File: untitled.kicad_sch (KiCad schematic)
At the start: 6 parts, among them J10 Conn_01x04_Male, J11 Conn_01x04_Male, J2 Conn_01x07_Male, J3 Conn_01x08_Male, J8 Conn_01x05_Male, J9 Conn_01x07_Male

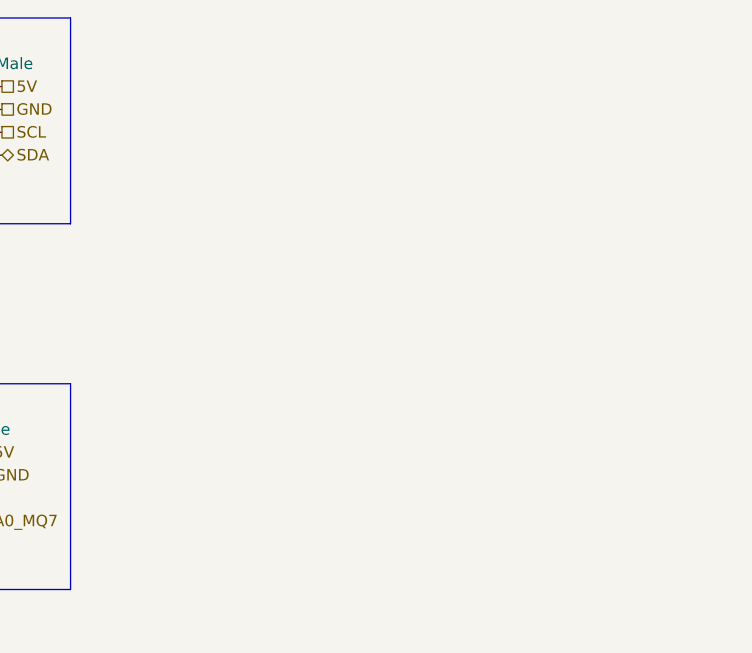
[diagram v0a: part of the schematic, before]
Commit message: Added some MQs
needs to be further investigated - to check if it is worth it to install also plain MQ
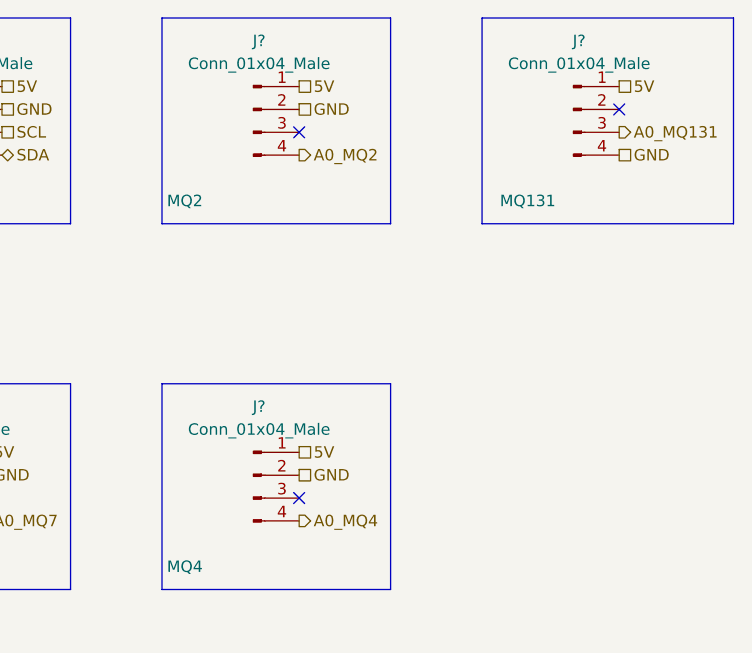
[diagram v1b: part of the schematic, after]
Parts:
- added J? (x3): Conn_01x04_Male, Connector_PinSocket_2.54mm:PinSocket_1x04_P2.54mm_Vertical, symbol Connector:Conn_01x04_Male
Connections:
- net 5V: now also J?.1 (Pin_1), J?.1 (Pin_1), J?.1 (Pin_1)
- net GND: now also J?.2 (Pin_2), J?.2 (Pin_2), J?.4 (Pin_4)
- new net A0_MQ131: J?.3 (Pin_3)
- new net A0_MQ2: J?.4 (Pin_4)
- new net A0_MQ4: J?.4 (Pin_4)
- no-connect marks 12 -> 15
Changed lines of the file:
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@@
   (no_connect (at 45.72 88.9))
   (no_connect (at 45.72 91.44))
+  (no_connect (at 147.32 43.18))
   (no_connect (at 76.2 43.18))
   (no_connect (at 43.18 53.34))
   (no_connect (at 43.18 40.64))
   (no_connect (at 76.2 88.9))
+  (no_connect (at 147.32 83.82))
+  (no_connect (at 182.88 40.64))
   (no_connect (at 76.2 91.44))
   (no_connect (at 111.76 83.82))
@@
     (stroke (width 0) (type default) (color 0 0 0 0))
   )
+  (polyline (pts (xy 157.48 53.34) (xy 157.48 30.48))
+    (stroke (width 0) (type default) (color 0 0 0 0))
+  )
+  (polyline (pts (xy 157.48 93.98) (xy 157.48 71.12))
+    (stroke (width 0) (type default) (color 0 0 0 0))
+  )
+  (polyline (pts (xy 132.08 71.12) (xy 132.08 93.98))
+    (stroke (width 0) (type default) (color 0 0 0 0))
+  )
   (polyline (pts (xy 60.96 68.58) (xy 60.96 96.52))
     (stroke (width 0) (type default) (color 0 0 0 0))
   )
+  (polyline (pts (xy 132.08 93.98) (xy 157.48 93.98))
+    (stroke (width 0) (type default) (color 0 0 0 0))
+  )
   (polyline (pts (xy 60.96 58.42) (xy 83.82 58.42))
     (stroke (width 0) (type default) (color 0 0 0 0))
@@
     (stroke (width 0) (type default) (color 0 0 0 0))
   )
+  (polyline (pts (xy 132.08 53.34) (xy 157.48 53.34))
+    (stroke (width 0) (type default) (color 0 0 0 0))
+  )
   (polyline (pts (xy 96.52 71.12) (xy 96.52 93.98))
     (stroke (width 0) (type default) (color 0 0 0 0))
@@
     (stroke (width 0) (type default) (color 0 0 0 0))
   )
+  (polyline (pts (xy 167.64 53.34) (xy 195.58 53.34))
+    (stroke (width 0) (type default) (color 0 0 0 0))
+  )
   (polyline (pts (xy 99.06 30.48) (xy 99.06 53.34))
     (stroke (width 0) (type default) (color 0 0 0 0))
@@
     (stroke (width 0) (type default) (color 0 0 0 0))
   )
+  (polyline (pts (xy 132.08 30.48) (xy 157.48 30.48))
+    (stroke (width 0) (type default) (color 0 0 0 0))
+  )
   (polyline (pts (xy 60.96 58.42) (xy 60.96 30.48))
     (stroke (width 0) (type default) (color 0 0 0 0))
   )
+  (polyline (pts (xy 195.58 53.34) (xy 195.58 30.48))
+    (stroke (width 0) (type default) (color 0 0 0 0))
+  )
   (polyline (pts (xy 86.36 96.52) (xy 60.96 96.52))
     (stroke (width 0) (type default) (color 0 0 0 0))
@@
     (stroke (width 0) (type default) (color 0 0 0 0))
   )
+  (polyline (pts (xy 132.08 71.12) (xy 157.48 71.12))
+    (stroke (width 0) (type default) (color 0 0 0 0))
+  )
   (polyline (pts (xy 30.48 68.58) (xy 30.48 99.06))
     (stroke (width 0) (type default) (color 0 0 0 0))
@@
     (stroke (width 0) (type default) (color 0 0 0 0))
   )
+  (polyline (pts (xy 132.08 30.48) (xy 132.08 53.34))
+    (stroke (width 0) (type default) (color 0 0 0 0))
+  )
   (polyline (pts (xy 53.34 68.58) (xy 30.48 68.58))
     (stroke (width 0) (type default) (color 0 0 0 0))
   )
+  (polyline (pts (xy 167.64 30.48) (xy 195.58 30.48))
+    (stroke (width 0) (type default) (color 0 0 0 0))
+  )
+  (polyline (pts (xy 167.64 30.48) (xy 167.64 53.34))
+    (stroke (width 0) (type default) (color 0 0 0 0))
+  )
   (polyline (pts (xy 53.34 58.42) (xy 27.94 58.42))
     (stroke (width 0) (type default) (color 0 0 0 0))
@@
     (effects (font (size 1.27 1.27)) (justify left))
   )
+  (hierarchical_label "A0_MQ4" (shape output) (at 147.32 86.36 0)
+    (effects (font (size 1.27 1.27)) (justify left))
+  )
   (hierarchical_label "5V" (shape passive) (at 114.3 38.1 0)
     (effects (font (size 1.27 1.27)) (justify left))
   )
+  (hierarchical_label "A0_MQ131" (shape output) (at 182.88 43.18 0)
+    (effects (font (size 1.27 1.27)) (justify left))
+  )
+  (hierarchical_label "GND" (shape passive) (at 147.32 81.28 0)
+    (effects (font (size 1.27 1.27)) (justify left))
+  )
   (hierarchical_label "5V" (shape passive) (at 111.76 78.74 0)
     (effects (font (size 1.27 1.27)) (justify left))
@@
     (effects (font (size 1.27 1.27)) (justify left))
   )
+  (hierarchical_label "A0_MQ2" (shape output) (at 147.32 45.72 0)
+    (effects (font (size 1.27 1.27)) (justify left))
+  )
   (hierarchical_label "5V" (shape passive) (at 76.2 76.2 0)
     (effects (font (size 1.27 1.27)) (justify left))
@@
     (effects (font (size 1.27 1.27)) (justify left))
   )
+  (hierarchical_label "5V" (shape passive) (at 147.32 38.1 0)
+    (effects (font (size 1.27 1.27)) (justify left))
+  )
+  (hierarchical_label "5V" (shape passive) (at 182.88 38.1 0)
+    (effects (font (size 1.27 1.27)) (justify left))
+  )
   (hierarchical_label "5V" (shape passive) (at 43.18 38.1 0)
     (effects (font (size 1.27 1.27)) (justify left))
@@
     (effects (font (size 1.27 1.27)) (justify left))
   )
+  (hierarchical_label "5V" (shape passive) (at 147.32 78.74 0)
+    (effects (font (size 1.27 1.27)) (justify left))
+  )
+  (hierarchical_label "GND" (shape passive) (at 182.88 45.72 0)
+    (effects (font (size 1.27 1.27)) (justify left))
+  )
   (hierarchical_label "SDA" (shape bidirectional) (at 114.3 45.72 0)
     (effects (font (size 1.27 1.27)) (justify left))
   )
   (hierarchical_label "GND" (shape passive) (at 76.2 45.72 0)
+    (effects (font (size 1.27 1.27)) (justify left))
+  )
+  (hierarchical_label "GND" (shape passive) (at 147.32 40.64 0)
     (effects (font (size 1.27 1.27)) (justify left))
   )
@@
     (pin "4")
     (pin "5")
+  )
+  (symbol (lib_id "Connector:Conn_01x04_Male") (at 177.8 40.64 0) (unit 1)
+    (in_bom yes) (on_board yes)
+    (property "Reference" "J?" (id 0) (at 178.435 33.02 0))
+    (property "Value" "Conn_01x04_Male" (id 1) (at 178.435 35.56 0))
+    (property "Footprint" "Connector_PinSocket_2.54mm:PinSocket_1x04_P2.54mm_Vertical" (id 2) (at 177.8 40.64 0)
+      (effects (font (size 1.27 1.27)) hide)
+    )
+    (property "Datasheet" "~" (id 3) (at 177.8 40.64 0)
+      (effects (font (size 1.27 1.27)) hide)
+    )
+    (property "Purpose" "MQ131" (id 4) (at 172.72 50.8 0))
+    (pin "1")
+    (pin "2")
+    (pin "3")
+    (pin "4")
   )
   (symbol (lib_id "Connector:Conn_01x07_Male") (at 38.1 45.72 0) (unit 1)
@@
     (pin "7")
   )
+  (symbol (lib_id "Connector:Conn_01x04_Male") (at 142.24 81.28 0) (unit 1)
+    (in_bom yes) (on_board yes)
+    (property "Reference" "J?" (id 0) (at 142.875 73.66 0))
+    (property "Value" "Conn_01x04_Male" (id 1) (at 142.875 76.2 0))
+    (property "Footprint" "Connector_PinSocket_2.54mm:PinSocket_1x04_P2.54mm_Vertical" (id 2) (at 142.24 81.28 0)
+      (effects (font (size 1.27 1.27)) hide)
+    )
+    (property "Datasheet" "~" (id 3) (at 142.24 81.28 0)
+      (effects (font (size 1.27 1.27)) hide)
+    )
+    (property "Purpose" "MQ4" (id 4) (at 134.62 91.44 0))
+    (pin "1")
+    (pin "2")
+    (pin "3")
+    (pin "4")
+  )
   (symbol (lib_id "Connector:Conn_01x04_Male") (at 106.68 81.28 0) (unit 1)
     (in_bom yes) (on_board yes)
@@
     (pin "1")
     (pin "2")
+    (pin "3")
+    (pin "4")
+  )
+  (symbol (lib_id "Connector:Conn_01x04_Male") (at 142.24 40.64 0) (unit 1)
+    (in_bom yes) (on_board yes)
+    (property "Reference" "J?" (id 0) (at 142.875 33.02 0))
+    (property "Value" "Conn_01x04_Male" (id 1) (at 142.875 35.56 0))
+    (property "Footprint" "Connector_PinSocket_2.54mm:PinSocket_1x04_P2.54mm_Vertical" (id 2) (at 142.24 40.64 0)
+      (effects (font (size 1.27 1.27)) hide)
+    )
+    (property "Datasheet" "~" (id 3) (at 142.24 40.64 0)
+      (effects (font (size 1.27 1.27)) hide)
+    )
+    (property "Purpose" "MQ2" (id 4) (at 134.62 50.8 0))
+    (pin "1")
+    (pin "2")

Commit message: Rearrangement
in order to fit all the new female pin sockets and fit all into a smaller PCB
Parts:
- gave numbers to parts that had none: 3
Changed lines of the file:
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@@
   (symbol (lib_id "Connector:Conn_01x04_Male") (at 177.8 40.64 0) (unit 1)
     (in_bom yes) (on_board yes)
-    (property "Reference" "J?" (id 0) (at 178.435 33.02 0))
+    (property "Reference" "J14" (id 0) (at 178.435 33.02 0))
     (property "Value" "Conn_01x04_Male" (id 1) (at 178.435 35.56 0))
     (property "Footprint" "Connector_PinSocket_2.54mm:PinSocket_1x04_P2.54mm_Vertical" (id 2) (at 177.8 40.64 0)
@@
   (symbol (lib_id "Connector:Conn_01x04_Male") (at 142.24 81.28 0) (unit 1)
     (in_bom yes) (on_board yes)
-    (property "Reference" "J?" (id 0) (at 142.875 73.66 0))
+    (property "Reference" "J13" (id 0) (at 142.875 73.66 0))
     (property "Value" "Conn_01x04_Male" (id 1) (at 142.875 76.2 0))
     (property "Footprint" "Connector_PinSocket_2.54mm:PinSocket_1x04_P2.54mm_Vertical" (id 2) (at 142.24 81.28 0)
@@
   (symbol (lib_id "Connector:Conn_01x04_Male") (at 142.24 40.64 0) (unit 1)
     (in_bom yes) (on_board yes)
-    (property "Reference" "J?" (id 0) (at 142.875 33.02 0))
+    (property "Reference" "J12" (id 0) (at 142.875 33.02 0))
     (property "Value" "Conn_01x04_Male" (id 1) (at 142.875 35.56 0))
     (property "Footprint" "Connector_PinSocket_2.54mm:PinSocket_1x04_P2.54mm_Vertical" (id 2) (at 142.24 40.64 0)

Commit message: Design tweaking
staging of all the modifications needed , in order to cover the needs of all the power board
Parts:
- removed J11, J13: Conn_01x04_Male, Connector_PinSocket_2.54mm:PinSocket_1x04_P2.54mm_Vertical, symbol Connector:Conn_01x04_Male
- added J5: Conn_01x04_Male, Connector_PinSocket_2.54mm:PinSocket_1x04_P2.54mm_Vertical, symbol Connector:Conn_01x04_Male
- J10: value Conn_01x04_Male -> Conn_01x04; Purpose MQ7 -> MQ4 / MQ7
- J12, J14: value Conn_01x04_Male -> Conn_01x04
- J2, J9: value Conn_01x07_Male -> Conn_01x07
- J3: value Conn_01x08_Male -> Conn_01x08
- J8: value Conn_01x05_Male -> Conn_01x05; Purpose SGP40 -> SGP40 / BMP180
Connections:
- net GND: now also J5.2 (Pin_2)
- net 5V renamed VCCA
- net VCCA: no longer J10.1 (Pin_1), J12.1 (Pin_1), J14.1 (Pin_1)
- net A0_MQ7 renamed A0_MQ47
- new net Rx: J5.3 (Pin_3)
- new net Tx: J5.4 (Pin_4)
- new net VCCB: J10.1 (Pin_1), J12.1 (Pin_1), J14.1 (Pin_1), J5.1 (Pin_1)
- no-connect marks 15 -> 14
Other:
- title: (none) -> PCB power supply for sensors
- moved on the sheet: J10, J12, J14, J2, J3, J8, J9

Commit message: Clear separation of 2 designs : with usb
consumption calculation , manuals / issue with slider switch to be checked if ok
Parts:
- J10, J14: Consumption (none) -> 150 mA
- J12: Consumption (none) -> 88 mA
- J2: Consumption (none) -> 12 mA
- J3: Consumption (none) -> 0,2 mA
- J8: Consumption (none) -> 4 mA
- J9: Consumption (none) -> 100 mA
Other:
- note added: "Roughly : power sup 600 mA"
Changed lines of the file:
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@@
     (stroke (width 0) (type default) (color 0 0 0 0))
+  )
+  (text "Roughly : power sup 600 mA" (at 76.2 50.8 0)
+    (effects (font (size 4 4) (thickness 0.8) bold) (justify left bottom))
   )
   (hierarchical_label "Tx" (shape output) (at 195.58 111.76 0)
@@
       (effects (font (size 1.27 1.27)) hide)
     )
-    (property "Datasheet" "~" (id 3) (at 119.38 71.12 0)
+    (property "Datasheet" "https://docs.rs-online.com/1956/A700000007055193.pdf" (id 3) (at 119.38 71.12 0)
       (effects (font (size 1.27 1.27)) hide)
     )
     (property "Purpose" "SGP40 / BMP180" (id 4) (at 119.38 81.28 0))
+    (property "Consumption" "4 mA" (id 5) (at 119.38 71.12 0)
+      (effects (font (size 1.27 1.27)) hide)
+    )
     (pin "1")
     (pin "2")
@@
     )
     (property "Purpose" "MQ131" (id 4) (at 182.88 81.28 0))
+    (property "Consumption" "150 mA" (id 5) (at 187.96 71.12 0)
+      (effects (font (size 1.27 1.27)) hide)
+    )
     (pin "1")
     (pin "2")
@@
       (effects (font (size 1.27 1.27)) hide)
     )
-    (property "Datasheet" "~" (id 3) (at 86.36 71.12 0)
+    (property "Datasheet" "https://cdn-shop.adafruit.com/product-files/3660/BME680.pdf" (id 3) (at 86.36 71.12 0)
       (effects (font (size 1.27 1.27)) hide)
     )
     (property "Purpose" "BME680" (id 4) (at 81.28 81.28 0))
+    (property "Consumption" "12 mA" (id 5) (at 86.36 71.12 0)
+      (effects (font (size 1.27 1.27)) hide)
+    )
     (pin "1")
     (pin "2")
@@
       (effects (font (size 1.27 1.27)) hide)
     )
-    (property "Datasheet" "~" (id 3) (at 88.9 109.22 0)
+    (property "Datasheet" "https://ww1.microchip.com/downloads/en/DeviceDoc/25095A.pdf" (id 3) (at 88.9 109.22 0)
       (effects (font (size 1.27 1.27)) hide)
     )
     (property "Purpose" "MCP9808" (id 4) (at 86.36 121.92 0))
+    (property "Consumption" "0,2 mA" (id 5) (at 88.9 109.22 0)
+      (effects (font (size 1.27 1.27)) hide)
+    )
     (pin "1")
     (pin "2")
@@
       (effects (font (size 1.27 1.27)) hide)
     )
-    (property "Datasheet" "~" (id 3) (at 119.38 109.22 0)
+    (property "Datasheet" "https://cdn-shop.adafruit.com/product-files/4632/4505_PMSA003I_series_data_manual_English_V2.6.pdf" (id 3) (at 119.38 109.22 0)
       (effects (font (size 1.27 1.27)) hide)
     )
     (property "Purpose" "PMSA003I" (id 4) (at 116.84 119.38 0))
+    (property "Consumption" "100 mA" (id 5) (at 119.38 109.22 0)
+      (effects (font (size 1.27 1.27)) hide)
+    )
     (pin "1")
     (pin "2")
@@
     )
     (property "Purpose" "MQ4 / MQ7" (id 4) (at 149.86 116.84 0))
+    (property "Consumption" "150 mA" (id 5) (at 152.4 106.68 0)
+      (effects (font (size 1.27 1.27)) hide)
+    )
     (pin "1")
     (pin "2")
@@
     )
     (property "Purpose" "MQ2" (id 4) (at 144.78 81.28 0))
-    (pin "1")
-    (pin "2")
+    (property "Consumption" "88 mA" (id 5) (at 152.4 71.12 0)
+      (effects (font (size 1.27 1.27)) hide)
+    )
+    (pin "1")
+    (pin "2")

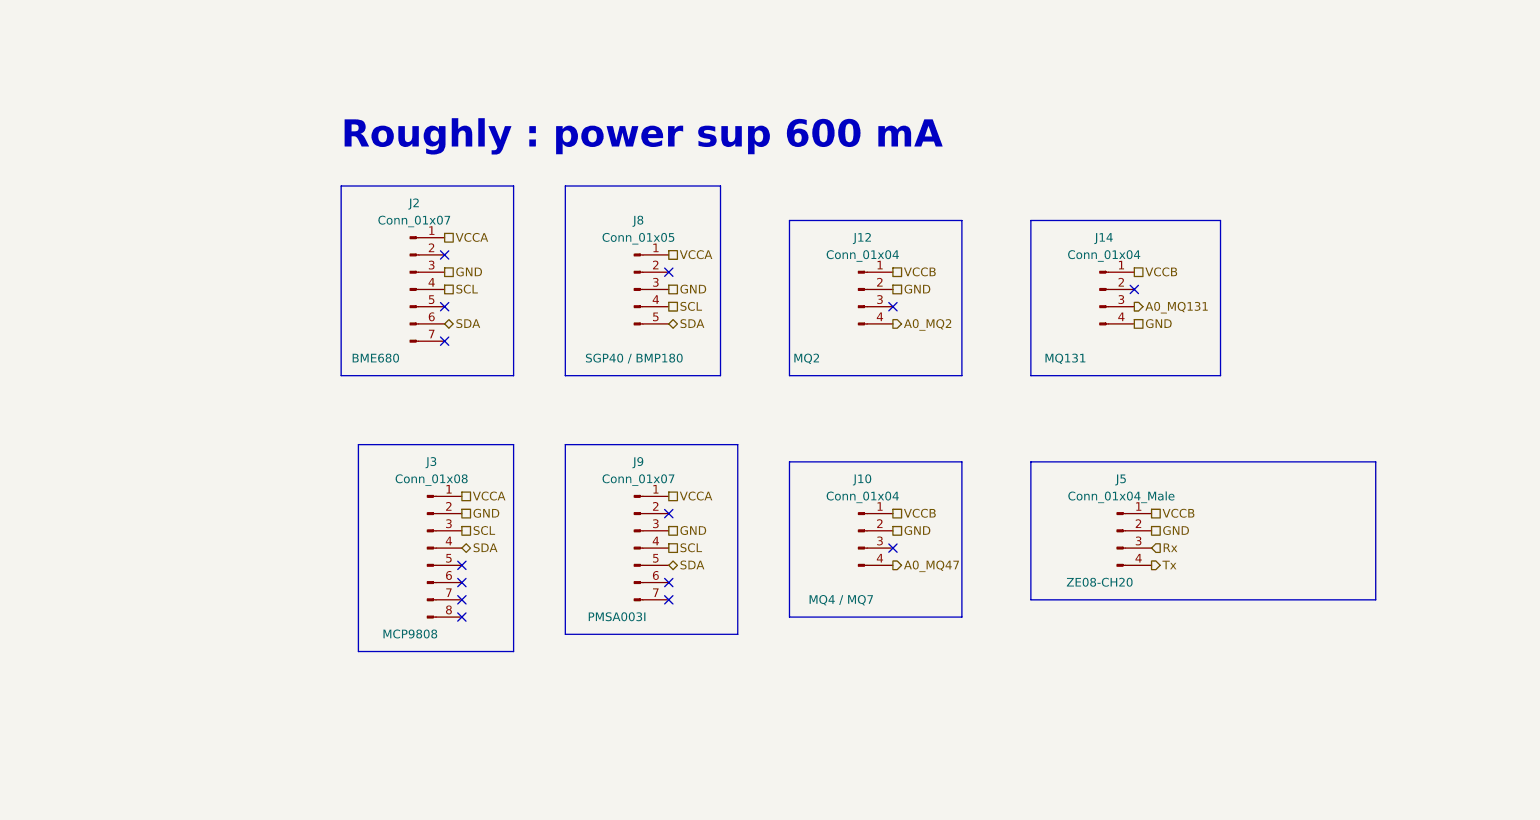
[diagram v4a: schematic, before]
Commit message: Design Rectified
Added pinheads & -sockets, all components and parts with their datasheets , power calculations and details - design improvement route tracks thickness check and calculation & F. silkscreening. Remaining : route tracks on the pcb
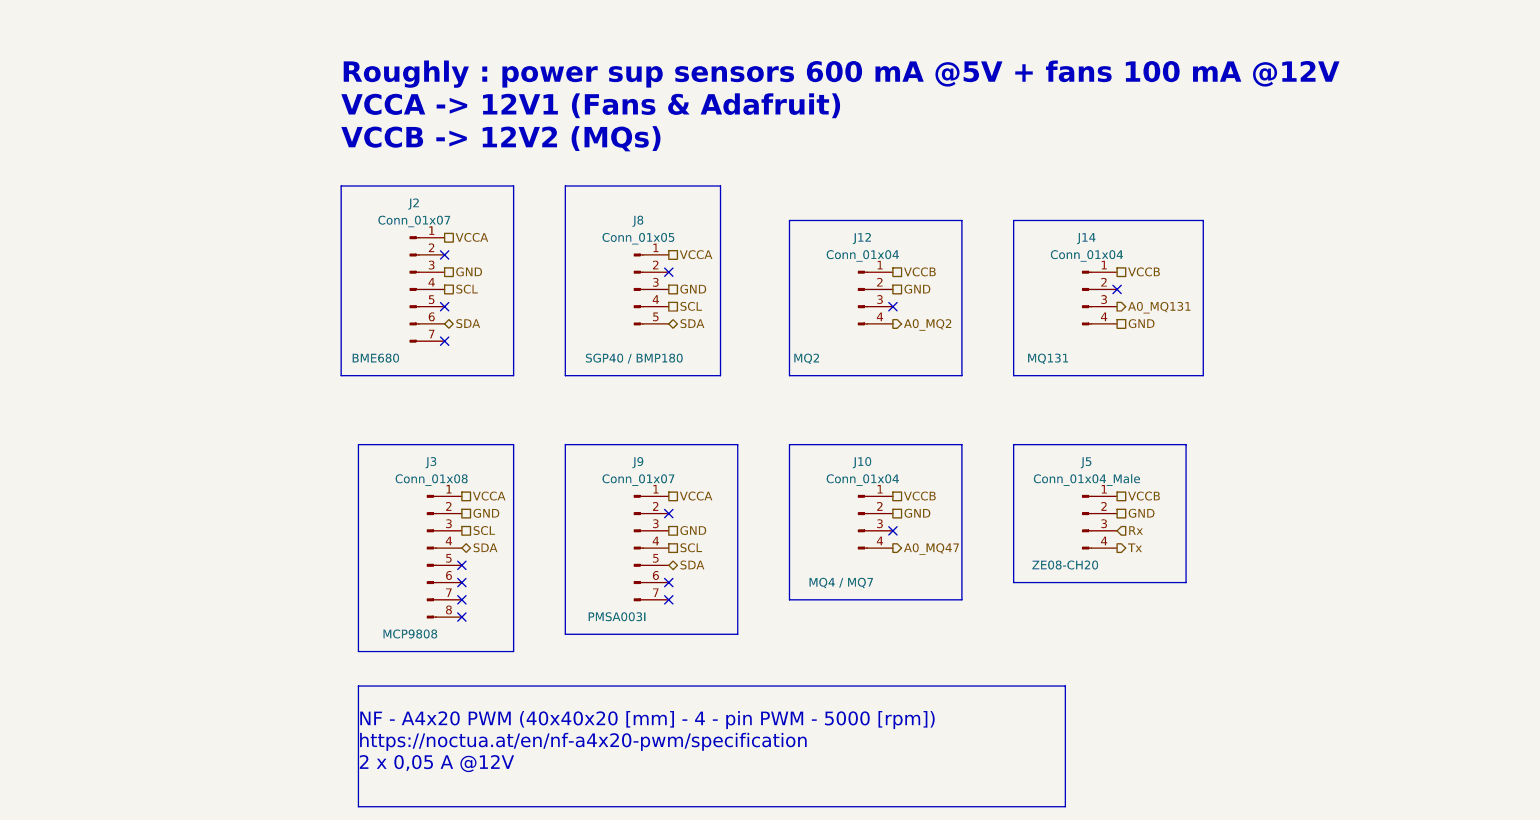
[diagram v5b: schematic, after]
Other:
- note added: "NF - A4x20 PWM (40x40x20 [mm] - 4 - pin PWM - 5000 [rpm]) https://noctua.at/en/nf-a4x20-pwm/specification 2 x 0,05 A @12V"
- note added: "Roughly : power sup sensors 600 mA @5V + fans 100 mA @12V VCCA -> 12V1 (Fans & Adafruit) VCCB -> 12V2 (MQs)"
- note removed: "Roughly : power sup 600 mA"
- moved on the sheet: J10, J14, J5
